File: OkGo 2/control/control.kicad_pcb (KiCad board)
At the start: 2 copper layers, 90.5 x 51 mm, 59 parts, among them P102 BATT, P103 BATT_CASE, P105 KEYSW, P106 ARM_LED, P108 SMA, P201 CH1, P203 CH3, P205 CH2, P207 CH4, Q201 BSS138BK, Q202 BSS138BK, Q203 BSS138BK, Q204 BSS138BK, U101 MEJ2S0305SC, U102 ADP3335, U104 LCD_HD44780, U105 STM32F071CBT6, U106 RFM95W, U108 SWD, Y101 8MHz

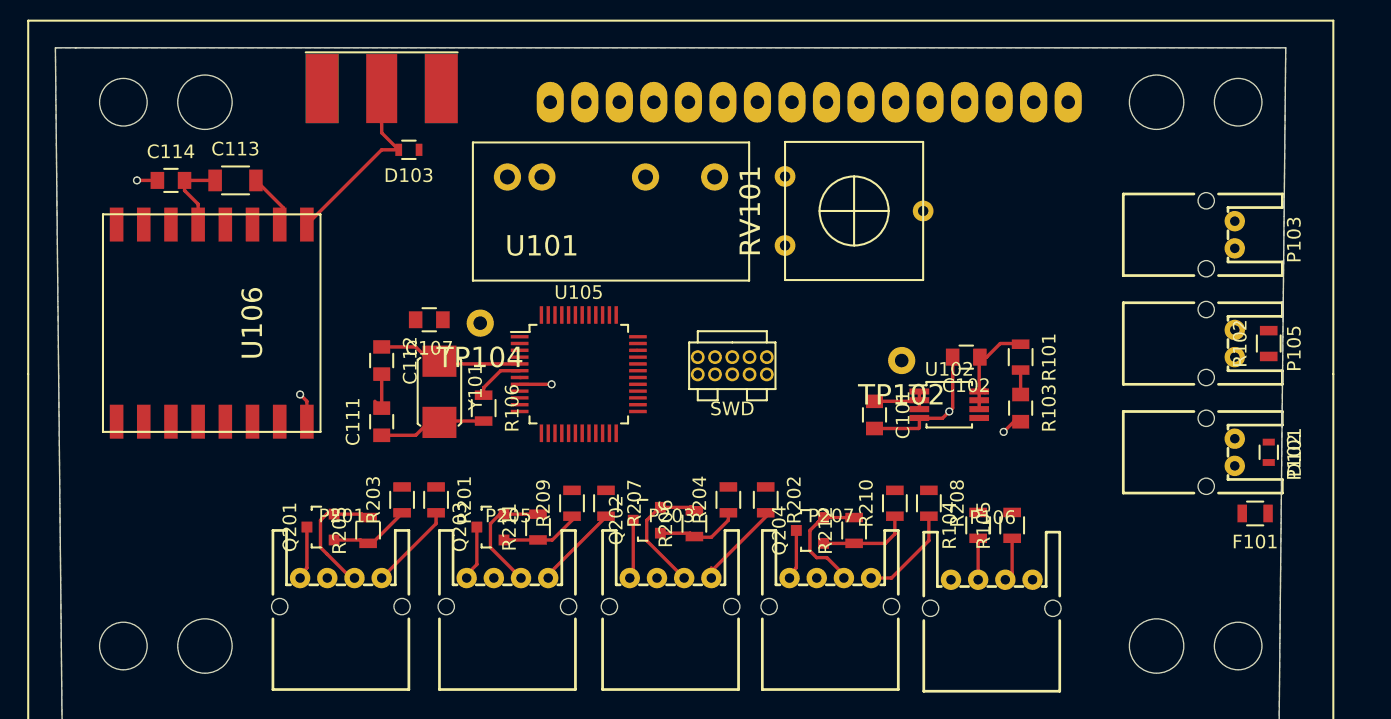
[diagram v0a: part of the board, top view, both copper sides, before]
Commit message: experimental routing of some of control
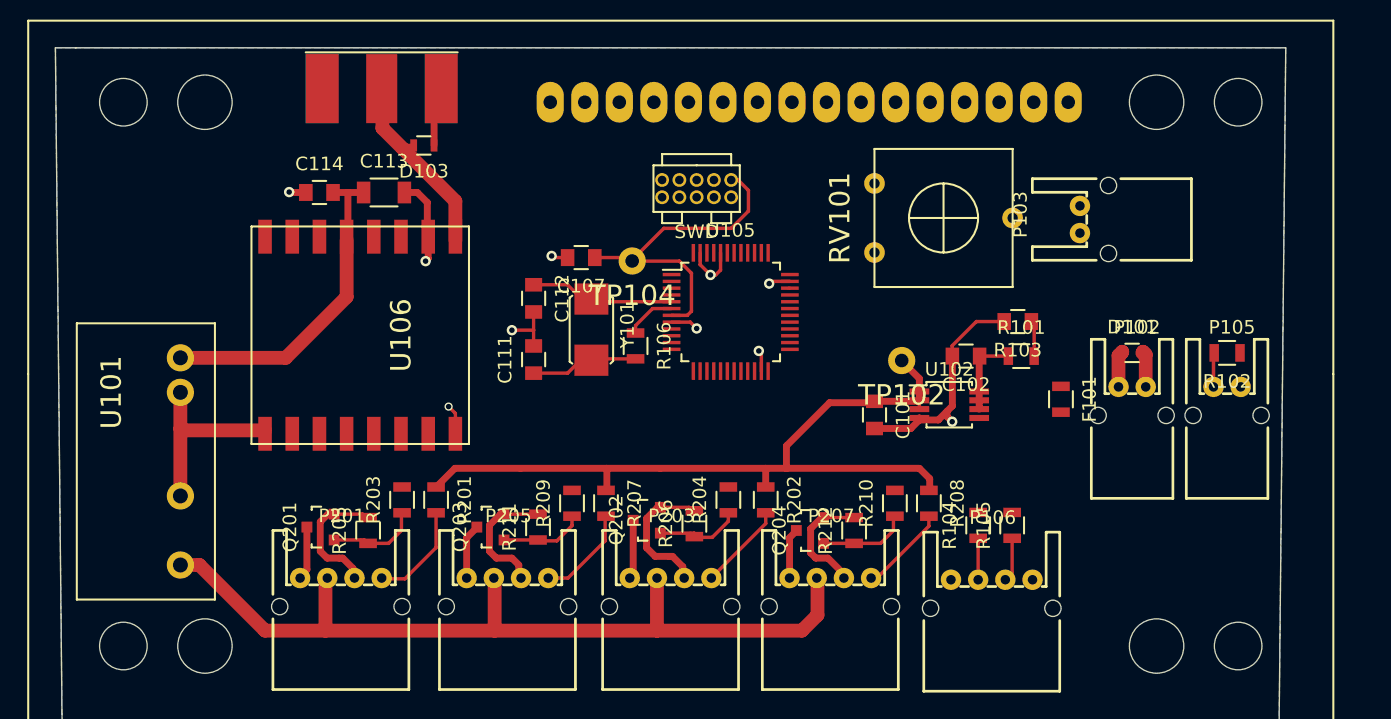
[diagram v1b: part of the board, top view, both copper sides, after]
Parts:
- moved U101 27.5 mm to (36.2, 58.8), turned to 270 degrees
- moved F101 16.6 mm to (101.0, 61.8), turned to 270 degrees
- moved U108 13.3 mm to (71.6, 45.7)
- moved D101 12.4 mm to (106.2, 58.4), turned to 0 degrees
- moved C107 12.1 mm to (65.7, 51.4)
- moved C111 12.1 mm to (62.2, 58.9)
- moved C112 12.1 mm to (62.2, 54.4)
- moved R106 12.1 mm to (69.7, 57.9)
- moved TP104 12.1 mm to (69.4, 51.7)
- moved U105 12.1 mm to (76.7, 55.4)
- moved Y101 12.1 mm to (66.4, 54.7)
- moved P103 11.8 mm to (102.4, 47.6), turned to 270 degrees
- moved C113 11.0 mm to (51.2, 46.6)
- moved C114 11.0 mm to (46.4, 46.6)
- moved U106 11.0 mm to (49.4, 57.1)
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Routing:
- net +3V3: track 11.4 -> 84.5 mm
- net +5V: track 0.00 -> 64.4 mm
- net GND: track 67.8 -> 106.0 mm, vias 5 -> 10
- net /nRST: track 0.10 -> 25.6 mm
- net Net-(D101-Pad1): track 0.00 -> 2.78 mm
- net /ARM_SW: track 0.00 -> 2.77 mm
- net Net-(D103-Pad2): track 14.8 -> 16.6 mm
- net Net-(Q201-Pad1): track 6.09 -> 7.80 mm
- net +BATT: track 7.74 -> 6.42 mm
- net Net-(P205-Pad4): track 5.33 -> 4.12 mm
- net Net-(P201-Pad1): track 6.71 -> 7.68 mm
- net Net-(P203-Pad4): track 5.31 -> 4.38 mm
- net Net-(Q202-Pad1): track 6.29 -> 7.09 mm
- net Net-(Q203-Pad1): track 6.23 -> 6.95 mm
- net Net-(P207-Pad1): track 7.44 -> 6.76 mm
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
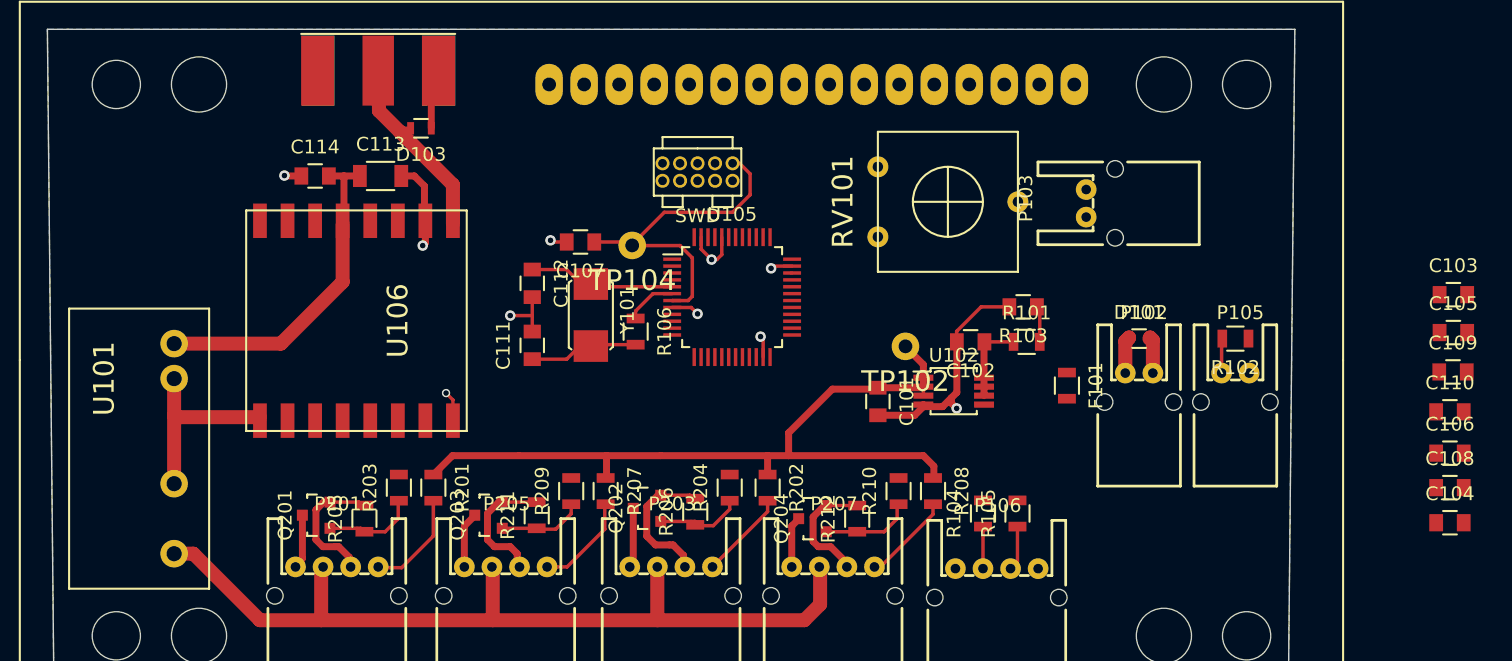
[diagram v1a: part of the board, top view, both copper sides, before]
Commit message: 4-bit LCD, pulldowns, 2-pin bicolour ARM LED
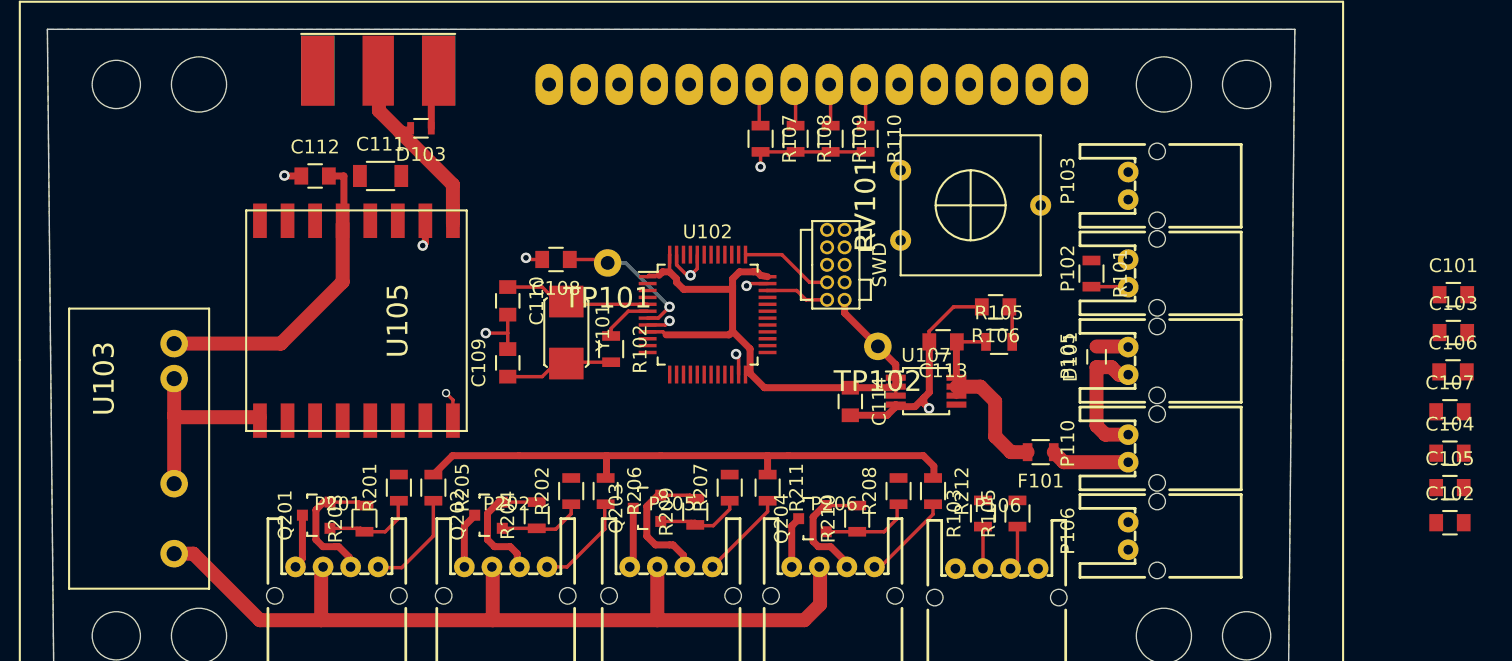
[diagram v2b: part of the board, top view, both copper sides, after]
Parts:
- added P106: ARM_LED, common:JST-PA-2, F.Cu at (105.4, 71.8)
- added P110: POWER_SW, common:JST-PA-2, F.Cu at (105.4, 65.4)
- added R107: 10k, Resistors_SMD:R_0805, F.Cu at (78.7, 43.9)
- added R108: 10k, Resistors_SMD:R_0805, F.Cu at (81.3, 43.9)
- added R109: 10k, Resistors_SMD:R_0805, F.Cu at (83.8, 43.9)
- added R110: 10k, Resistors_SMD:R_0805, F.Cu at (86.4, 43.9)
- R103: renamed from R104; value 68R -> 75R
- moved U101 15.5 mm to (83.6, 55.6), turned to 90 degrees
- moved P102 12.0 mm to (105.4, 52.7), turned to 270 degrees
- moved R101 11.5 mm to (102.7, 53.7), turned to 270 degrees
- moved F101 5.19 mm to (99.1, 66.7), turned to 180 degrees
- moved D101 3.36 mm to (103.1, 59.8), turned to 90 degrees
- moved P103 3.30 mm to (105.4, 46.4)
- moved P105 2.60 mm to (105.4, 59.1), turned to 270 degrees
- moved R102 2.18 mm to (67.9, 59.2)
- moved TP101 2.18 mm to (67.6, 52.9)
- moved U102 2.18 mm to (74.9, 56.7)
- moved Y101 2.18 mm to (64.6, 55.9)
- moved C108 2.18 mm to (63.9, 52.7)
- moved C109 2.18 mm to (60.4, 60.2)
- moved C110 2.18 mm to (60.4, 55.7)
- moved C113 2.00 mm to (92.0, 58.7)
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- renumbered C103 to C101, C104 to C102, C105 to C103, C106 to C104, C108 to C105, C109 to C106, C110 to C107, C107 to C108, C111 to C109, C112 to C110, C113 to C111, C114 to C112, C102 to C113, C101 to C114, P105 to P102, P102 to P105, P205 to P202, P203 to P205, P207 to P206, Q203 to Q202, Q202 to Q203, R102 to R101, R106 to R102, R101 to R105, R103 to R106, R203 to R201, R209 to R202, R205 to R203, R211 to R204, R201 to R205, R207 to R206, R204 to R207, R210 to R208, R206 to R209, R212 to R210, R202 to R211, R208 to R212, TP104 to TP101, U108 to U101, U105 to U102, U101 to U103, U106 to U105, U104 to U106, U102 to U107
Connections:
- C111 pad 1: +3V3 -> GND
- C111 pad 2: GND -> +3V3
- F101 pad 1: Net-(D101-Pad1) -> Net-(F101-Pad1)
- P103 pad 1: (no net) -> Net-(BT101-Pad1)
- P103 pad 2: (no net) -> Net-(BT101-Pad2)
- P106 pad 1: GND -> /DISARM_LED
- P106 pad 3: Net-(P106-Pad3) -> (no net)
- R103 pad 1: Net-(P106-Pad3) -> Net-(P106-Pad2)
- R103 pad 2: (no net) -> /ARM_LED
- R201 pad 2: (no net) -> /controls/CH1_LED
- R202 pad 2: (no net) -> /controls/CH2_LED
- R207 pad 2: (no net) -> /controls/CH3_LED
- R208 pad 2: (no net) -> /controls/CH4_LED
- U101 pad 6: (no net) -> Net-(U101-Pad6)
- U101 pad 7: (no net) -> Net-(U101-Pad7)
- U101 pad 8: (no net) -> Net-(U101-Pad8)
- U102 pad 10: (no net) -> Net-(U102-Pad10)
- U102 pad 11: (no net) -> Net-(U102-Pad11)
- U102 pad 12: (no net) -> Net-(U102-Pad12)
- U102 pad 13: (no net) -> Net-(U102-Pad13)
- U102 pad 14: (no net) -> Net-(U102-Pad14)
- U102 pad 15: (no net) -> Net-(U102-Pad15)
- U102 pad 16: (no net) -> Net-(U102-Pad16)
- U102 pad 17: (no net) -> Net-(U102-Pad17)
- U102 pad 18: (no net) -> Net-(U102-Pad18)
- U102 pad 19: (no net) -> Net-(U102-Pad19)
- U102 pad 20: (no net) -> Net-(U102-Pad20)
- U102 pad 21: (no net) -> Net-(U102-Pad21)
- U102 pad 22: (no net) -> Net-(U102-Pad22)
- U102 pad 25: (no net) -> Net-(U102-Pad25)
- U102 pad 26: (no net) -> Net-(U102-Pad26)
- U102 pad 27: (no net) -> Net-(U102-Pad27)
- U102 pad 28: (no net) -> Net-(U102-Pad28)
- U102 pad 29: (no net) -> Net-(U102-Pad29)
- U102 pad 3: (no net) -> Net-(U102-Pad3)
- U102 pad 30: (no net) -> Net-(U102-Pad30)
- U102 pad 31: (no net) -> Net-(U102-Pad31)
- U102 pad 32: (no net) -> Net-(U102-Pad32)
- U102 pad 33: (no net) -> Net-(U102-Pad33)
- U102 pad 38: (no net) -> Net-(U102-Pad38)
- U102 pad 39: (no net) -> Net-(U102-Pad39)
- U102 pad 4: (no net) -> Net-(U102-Pad4)
- U102 pad 40: (no net) -> Net-(U102-Pad40)
- U102 pad 41: (no net) -> Net-(U102-Pad41)
- U102 pad 42: (no net) -> Net-(U102-Pad42)
- U102 pad 43: (no net) -> Net-(U102-Pad43)
- U102 pad 45: (no net) -> Net-(U102-Pad45)
- U102 pad 46: (no net) -> Net-(U102-Pad46)
- U105 pad 11: (no net) -> /RFM_DIO3
- U105 pad 12: (no net) -> /RFM_DIO4
- U105 pad 14: (no net) -> /RFM_DIO0
- U105 pad 15: (no net) -> /RFM_DIO1
- U105 pad 16: (no net) -> /RFM_DIO2
- U105 pad 2: (no net) -> /RFM_MISO
- U105 pad 3: (no net) -> /RFM_MOSI
- U105 pad 4: (no net) -> /RFM_SCK
- U105 pad 5: (no net) -> /RFM_NSS
- U105 pad 6: (no net) -> /RFM_RESET
- U105 pad 7: (no net) -> /RFM_DIO5
- U106 pad 10: (no net) -> Net-(R107-Pad1)
- U106 pad 11: (no net) -> /LCD_DB4
- U106 pad 12: (no net) -> /LCD_DB5
- U106 pad 13: (no net) -> /LCD_DB6
- U106 pad 14: (no net) -> /LCD_DB7
- U106 pad 4: (no net) -> /LCD_RS
- U106 pad 6: (no net) -> /LCD_E
- U106 pad 7: (no net) -> Net-(R110-Pad1)
- U106 pad 8: (no net) -> Net-(R109-Pad1)
- U106 pad 9: (no net) -> Net-(R108-Pad1)
- U107 pad 5: (no net) -> Net-(U107-Pad5)
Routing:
- net +3V3: track 84.5 -> 111.1 mm
- net /nRST: track 25.6 -> 11.4 mm, vias 0 -> 1
- net +BATT: track 6.42 -> 15.0 mm
- net /SWDCLK: track 0.00 -> 6.75 mm
- net Net-(D101-Pad1): track 2.78 -> 9.33 mm
- net Net-(F101-Pad1): track 0.00 -> 5.70 mm
- net /SWDIO: track 0.10 -> 4.70 mm
- net Net-(P106-Pad3): track 3.05 -> 0.00 mm
- net Net-(P106-Pad2): track 3.26 -> 6.31 mm
- net Net-(R107-Pad1): track 0.00 -> 3.03 mm
- net Net-(R110-Pad1): track 0.00 -> 3.03 mm
- net Net-(R109-Pad1): track 0.00 -> 3.03 mm
- net Net-(R108-Pad1): track 0.00 -> 3.03 mm
- net GND: track 106.0 -> 109.0 mm, vias 10 -> 11

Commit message: Finished demo-route of control
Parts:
- removed the P106 at (98.9, 75.1)
- removed the P106 at (105.4, 71.8)
- removed the R105 at (97.4, 71.1)
- added P106: ARM_LED, common:JST-PA-2, F.Cu at (98.9, 75.1)
- moved R103 2.96 mm to (97.8, 71.6)
- moved C108 2.86 mm to (66.0, 50.8)
- moved TP101 2.39 mm to (69.6, 51.6)
- moved C112 2.34 mm to (44.6, 45.1)
- moved U105 2.34 mm to (47.6, 55.6)
- moved C111 2.18 mm to (49.5, 45.2), turned to 180 degrees
- moved R102 1.44 mm to (66.5, 59.7)
- moved R204 1.29 mm to (61.2, 71.4)
- moved REF** 1.27 mm to (74.3, 108.0)
- moved U106 1.27 mm to (74.3, 60.0)
- moved Y101 1.16 mm to (63.5, 56.1)
- moved R202 1.16 mm to (64.0, 70.1), turned to 0 degrees
- moved C114 1.11 mm to (86.4, 63.0)
- moved R203 0.99 mm to (49.0, 71.4)
- moved R212 0.92 mm to (91.9, 70.1), turned to 180 degrees
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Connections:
- P201 pad 1: Net-(P201-Pad1) -> /controls/CH1_SW
- P202 pad 1: Net-(P202-Pad1) -> /controls/CH2_SW
- P205 pad 1: Net-(P205-Pad1) -> /controls/CH3_SW
- P206 pad 1: Net-(P206-Pad1) -> /controls/CH4_SW
- R205 pad 2: Net-(P201-Pad1) -> /controls/CH1_SW
- R206 pad 2: Net-(P202-Pad1) -> /controls/CH2_SW
- R211 pad 2: Net-(P205-Pad1) -> /controls/CH3_SW
- R212 pad 2: Net-(P206-Pad1) -> /controls/CH4_SW
- U102 pad 10: Net-(U102-Pad10) -> /RFM_DIO1
- U102 pad 11: Net-(U102-Pad11) -> /RFM_DIO2
- U102 pad 12: Net-(U102-Pad12) -> /RFM_DIO5
- U102 pad 13: Net-(U102-Pad13) -> /RFM_RESET
- U102 pad 14: Net-(U102-Pad14) -> /RFM_NSS
- U102 pad 15: Net-(U102-Pad15) -> /RFM_SCK
- U102 pad 16: Net-(U102-Pad16) -> /RFM_MISO
- U102 pad 17: Net-(U102-Pad17) -> /RFM_MOSI
- U102 pad 18: Net-(U102-Pad18) -> /controls/CH1_LED
- U102 pad 19: Net-(U102-Pad19) -> /BATT_MON
- U102 pad 2: (no net) -> /RFM_DIO3
- U102 pad 20: Net-(U102-Pad20) -> /controls/CH1_SW
- U102 pad 21: Net-(U102-Pad21) -> /controls/CH2_LED
- U102 pad 22: Net-(U102-Pad22) -> /controls/CH2_SW
- U102 pad 25: Net-(U102-Pad25) -> /controls/CH3_LED
- U102 pad 26: Net-(U102-Pad26) -> /controls/CH3_SW
- U102 pad 27: Net-(U102-Pad27) -> /controls/CH4_LED
- U102 pad 28: Net-(U102-Pad28) -> /controls/CH4_SW
- U102 pad 29: Net-(U102-Pad29) -> /ARM_LED
- U102 pad 3: Net-(U102-Pad3) -> /RFM_DIO4
- U102 pad 30: Net-(U102-Pad30) -> /DISARM_LED
- U102 pad 31: Net-(U102-Pad31) -> /ARM_SW
- U102 pad 38: Net-(U102-Pad38) -> /LCD_RS
- U102 pad 39: Net-(U102-Pad39) -> /LCD_E
- U102 pad 4: Net-(U102-Pad4) -> /RFM_DIO0
- U102 pad 42: Net-(U102-Pad42) -> /LCD_DB4
- U102 pad 43: Net-(U102-Pad43) -> /LCD_DB5
- U102 pad 45: Net-(U102-Pad45) -> /LCD_DB6
- U102 pad 46: Net-(U102-Pad46) -> /LCD_DB7
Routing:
- net +3V3: track 111.1 -> 329.6 mm, vias 0 -> 6
- net +5V: track 64.4 -> 135.3 mm, vias 0 -> 3
- net /RFM_MOSI: track 0.00 -> 44.3 mm
- net /RFM_DIO2: track 0.00 -> 41.9 mm, vias 0 -> 2
- net /RFM_DIO1: track 0.00 -> 40.0 mm, vias 0 -> 2
- net /DISARM_LED: track 0.00 -> 36.8 mm, vias 0 -> 2
- net /RFM_MISO: track 0.00 -> 36.4 mm
- net /controls/CH1_SW: track 0.00 -> 34.3 mm
- net /RFM_SCK: track 0.00 -> 31.4 mm
- net /RFM_DIO0: track 0.00 -> 30.1 mm, vias 0 -> 2
- net /ARM_LED: track 0.00 -> 29.3 mm, vias 0 -> 2
- net /controls/CH4_SW: track 0.00 -> 29.2 mm, vias 0 -> 2
- net /RFM_RESET: track 0.00 -> 28.7 mm
- net /RFM_NSS: track 0.00 -> 28.3 mm
- net /RFM_DIO5: track 0.00 -> 28.2 mm, vias 0 -> 2
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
